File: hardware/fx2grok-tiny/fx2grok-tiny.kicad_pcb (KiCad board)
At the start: 2 copper layers, 13 x 13 mm, 28 parts, among them IC1 CY7C68013A-56, P1 CONN_01X05, P2 CONN_01X05, U1 MICRO-USB-B-SMD, U2 MIC5319, Y1 24MHz

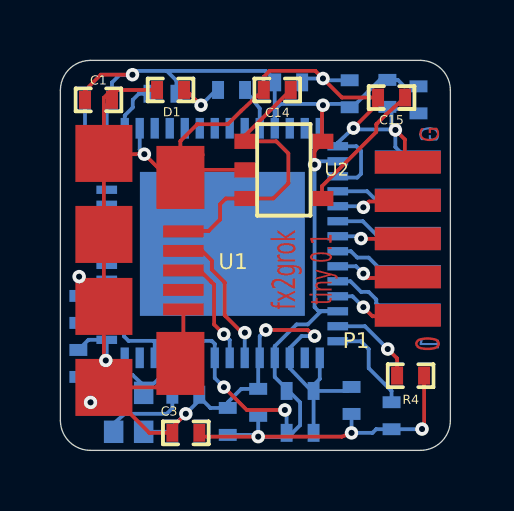
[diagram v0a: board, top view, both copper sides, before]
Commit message: layout: Update due to MIC5504 change, minor USB connector fixup.
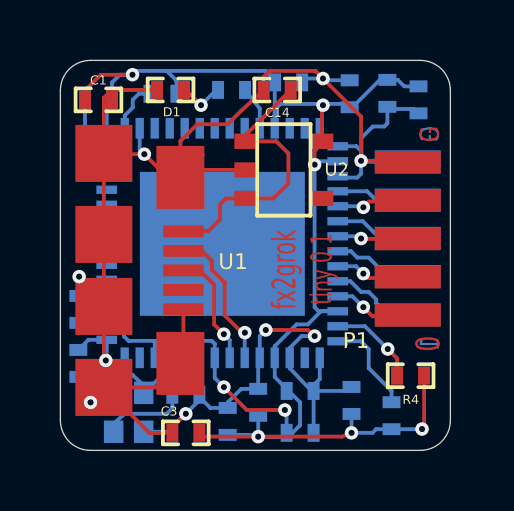
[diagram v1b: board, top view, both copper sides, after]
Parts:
- removed C15: 100nF, SM0402
- C16: value 2.2uF -> 1uF
- U2: value MIC5319 -> MIC5504
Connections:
- U2 pad 4: Net-(C15-Pad1) -> (no net)
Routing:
- net Net-(C15-Pad1): track 4.53 -> 0.00 mm
- net GND: track 77.6 -> 79.0 mm, vias 10 -> 9
